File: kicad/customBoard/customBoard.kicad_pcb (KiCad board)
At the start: 2 copper layers, 158.3 x 110 mm, 77 parts, among them J1 USB4125-GF-A_REVA2, J2 SS-53000-001, J3 FFC3B07-20-T, J4 Micro_SD_Card_Det, J5 ARJM11D7-502-AB-EW2, J6 SS-52100-001, J7 SS-52100-001, J8 SS-52100-001, J9 FFC3B07-20-T, Q1 MMUN2133LT1G, U1 TPS61090RSAR, U2 MCP73871-2CCI_ML, U3 74LVC1G07, U4 RT9742VGJ5, U5 RT9742ENGJ5, U6 TPD4EUSB30, U7 TPD4EUSB30, U8 USB2504A-JT, U9 AP22653W6-7, Y1 24MHz

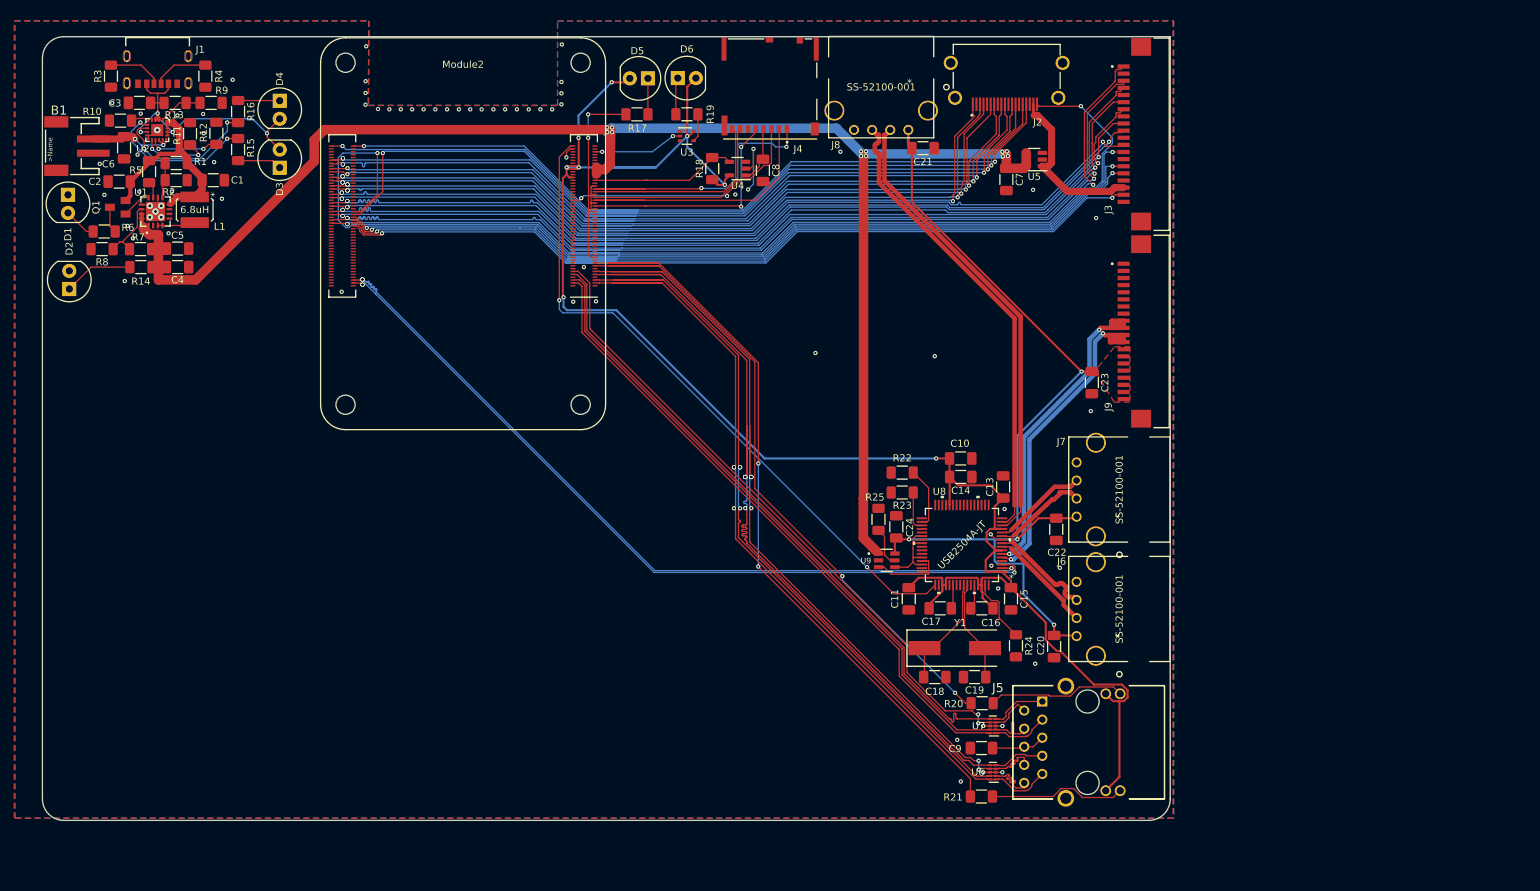
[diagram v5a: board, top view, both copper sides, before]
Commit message: Updates based on meeting with Dr. Jordan
Everything should be good to go now, next up is generating a bill of materials (making sure everything is in stock), and generating gerbers
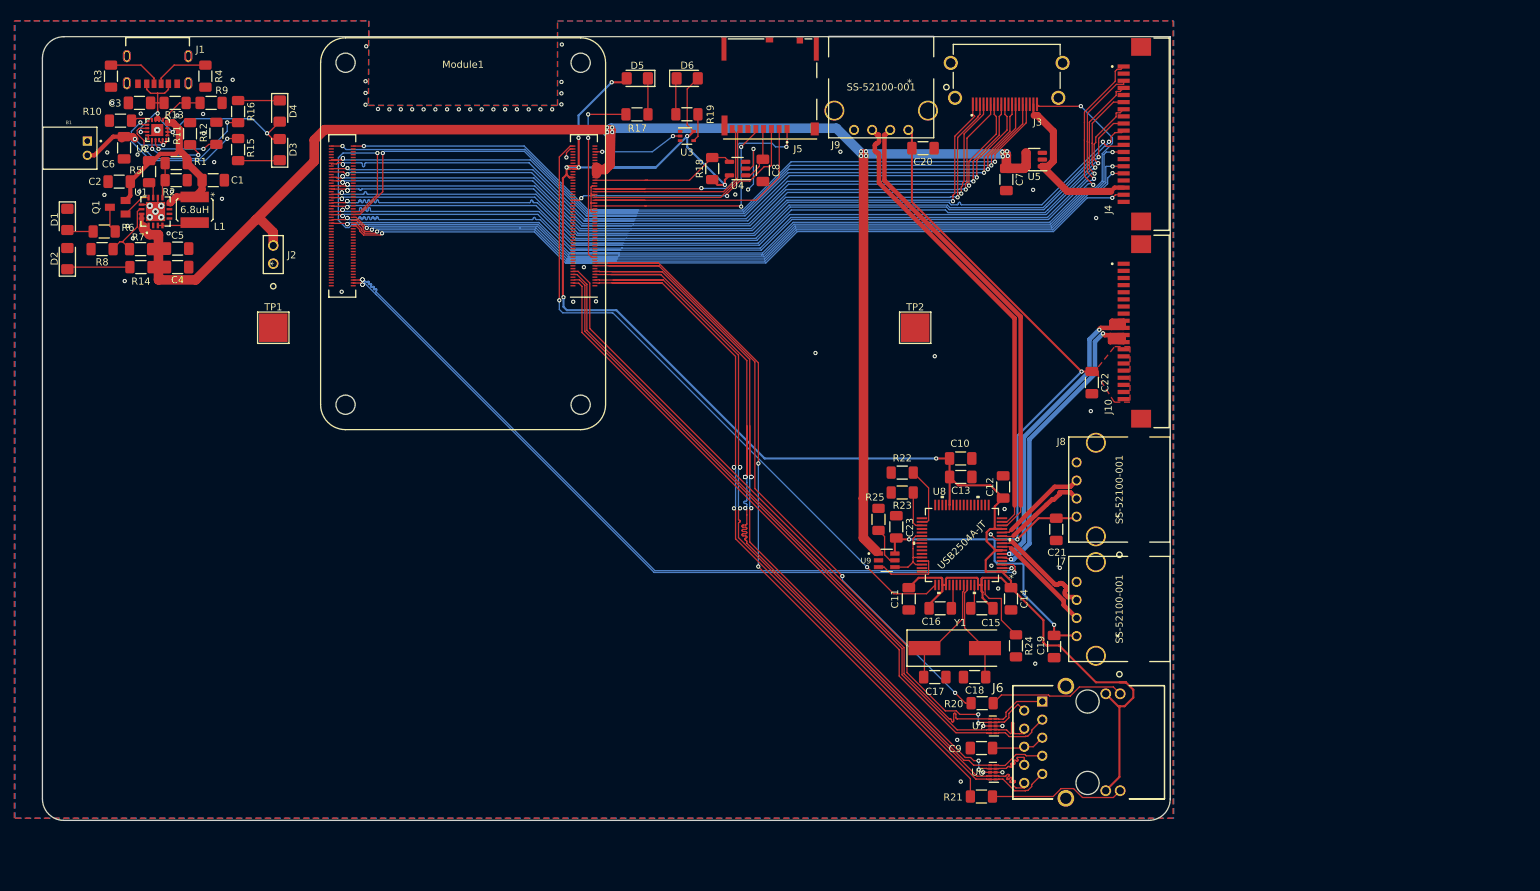
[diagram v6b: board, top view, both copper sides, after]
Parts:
- added J2: PREC002SAAN-RC, PREC002SAAN-RC:PREC002SAAN-RC, F.Cu at (59.8, 52.2)
- added TP1: TestPoint, TestPoint:TestPoint_Pad_4.0x4.0mm, F.Cu at (59.8, 61.2)
- added TP2: TestPoint, TestPoint:TestPoint_Pad_4.0x4.0mm, F.Cu at (149.9, 61.2)
- B1: footprint JSTPH2:JSTPH2 -> JST_S2B-PH-K-S(LF)(SN):JST_S2B-PH-K-S(LF)(SN)
- D1, D2, D3, D4, D5, D6: footprint digikey-footprints:LED_5mm_Radial -> LED_SMD:LED_1206_3216Metric_Pad1.42x1.75mm_HandSolder
- moved B1 2.87 mm to (33.7, 36.0), turned to -90 degrees
- moved D2 1.74 mm to (30.9, 51.5)
- moved D6 1.23 mm to (117.9, 26.2)
- moved D4 1.09 mm to (60.7, 30.8)
- moved D5 1.05 mm to (110.9, 26.2)
- moved D1 0.92 mm to (30.9, 46.0)
- renumbered C13 to C12, C14 to C13, C15 to C14, C16 to C15, C17 to C16, C18 to C17, C19 to C18, C20 to C19, C21 to C20, C22 to C21, C23 to C22, C24 to C23, J9 to J10, J2 to J3, J3 to J4, J4 to J5, J5 to J6, J6 to J7, J7 to J8, J8 to J9, Module2 to Module1
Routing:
- net /CM4/5v: track 215.2 -> 220.1 mm
- net +3V3: track 258.3 -> 261.2 mm
- net Net-(B1-Pad2): track 13.0 -> 15.3 mm
- net VBUS: track 44.1 -> 42.8 mm
- net Net-(D1-Pad2): track 4.61 -> 3.70 mm
- net Net-(D2-Pad1): track 9.77 -> 8.89 mm
- net Net-(D6-Pad1): track 4.69 -> 5.48 mm
- net Net-(R24-Pad1): track 9.27 -> 9.78 mm

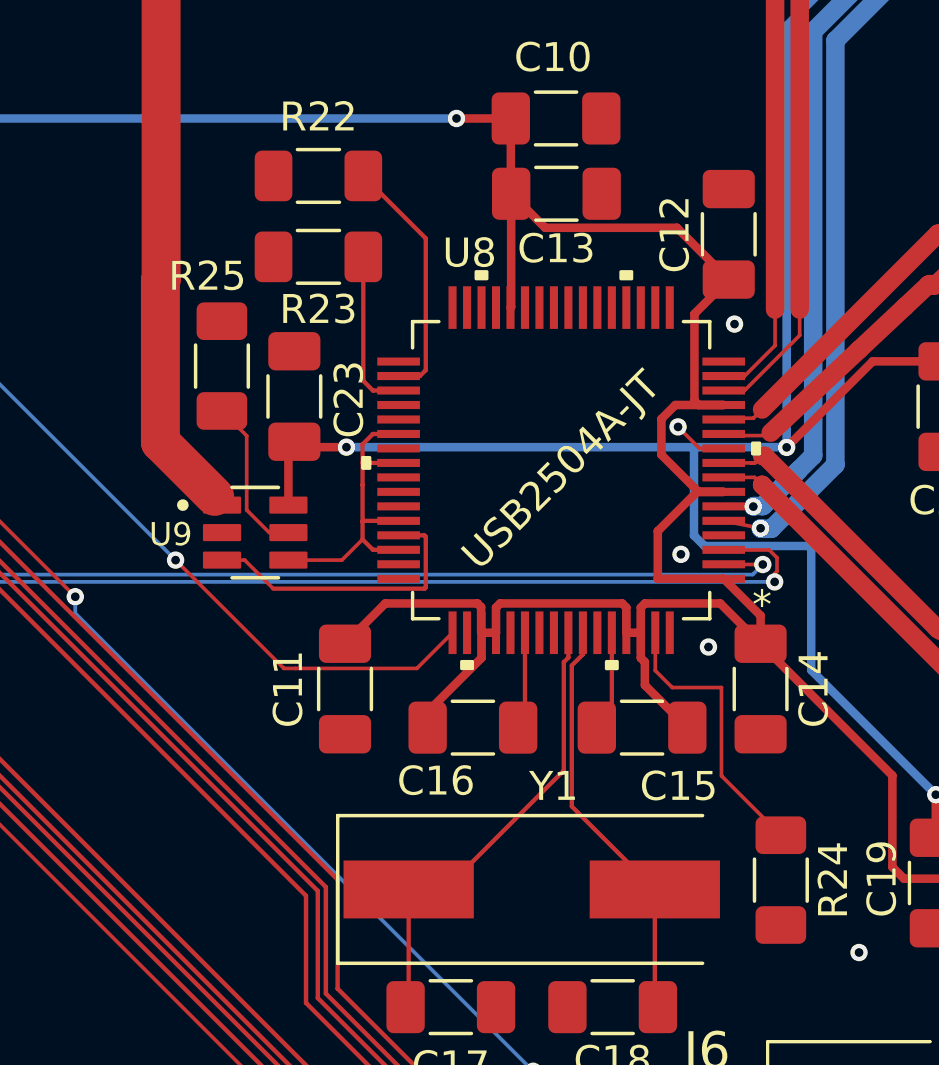
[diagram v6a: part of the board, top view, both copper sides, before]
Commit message: Generate BOM
Clean up all the part data and add manufacturer's numbers for ordering
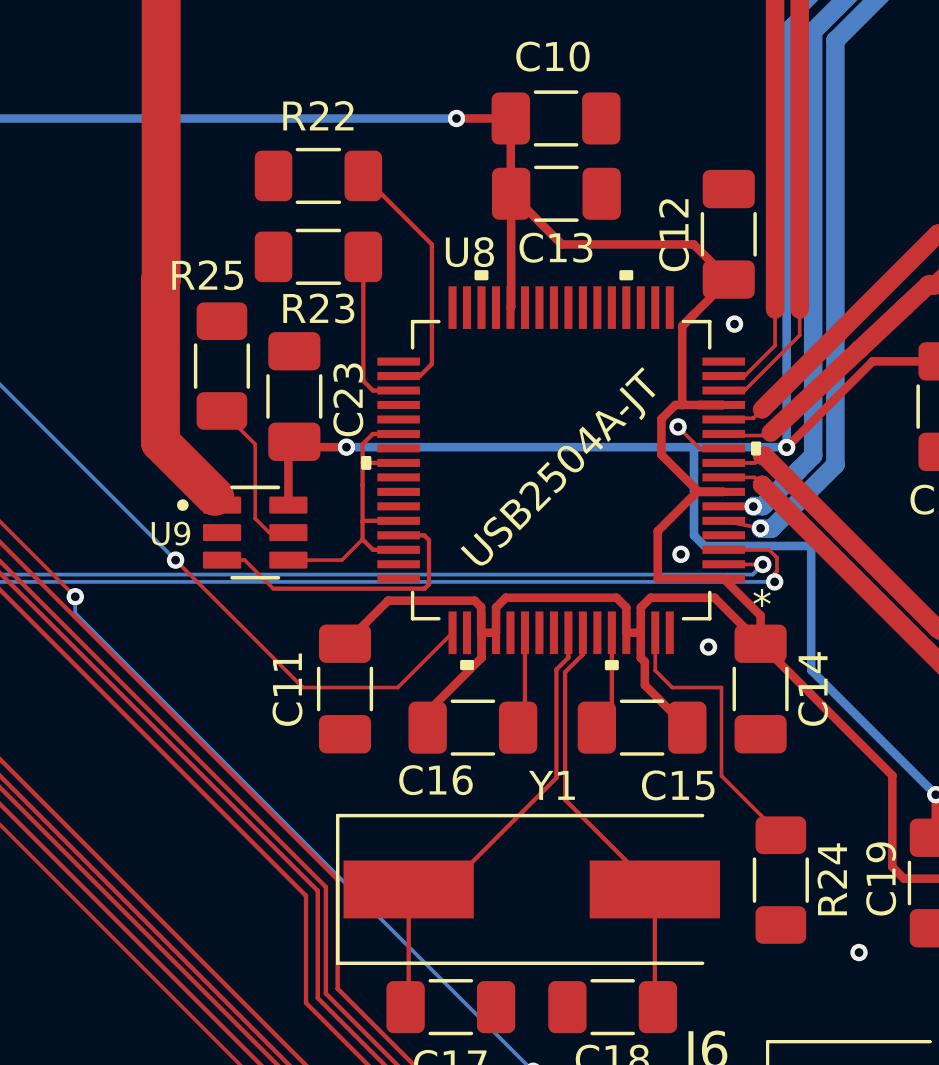
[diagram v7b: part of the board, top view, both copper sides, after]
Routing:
- net +3V3: track 261.2 -> 262.4 mm
- net /CM4/nEXTRST: track 93.8 -> 94.3 mm
